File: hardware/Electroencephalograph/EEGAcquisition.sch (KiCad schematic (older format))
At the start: 52 parts, among them U1 ADS1298IPAG, U2 OPA330xxD, U4 REF5025, U5 OPA350, X1 2M048

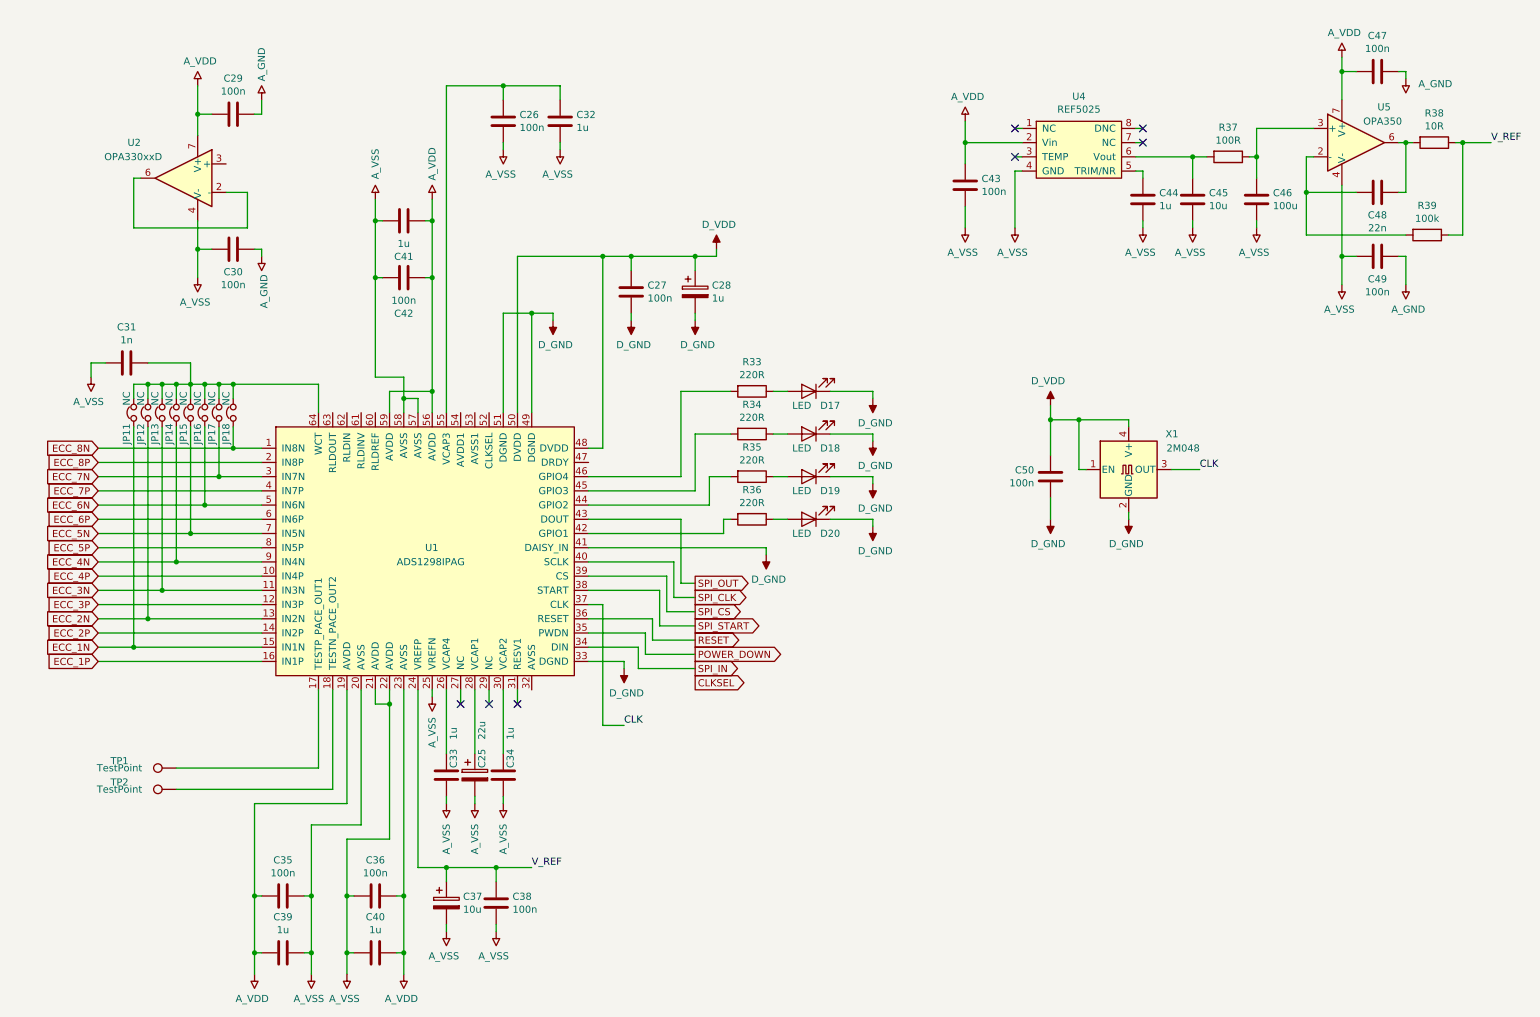
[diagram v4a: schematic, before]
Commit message: removed external clk and vref
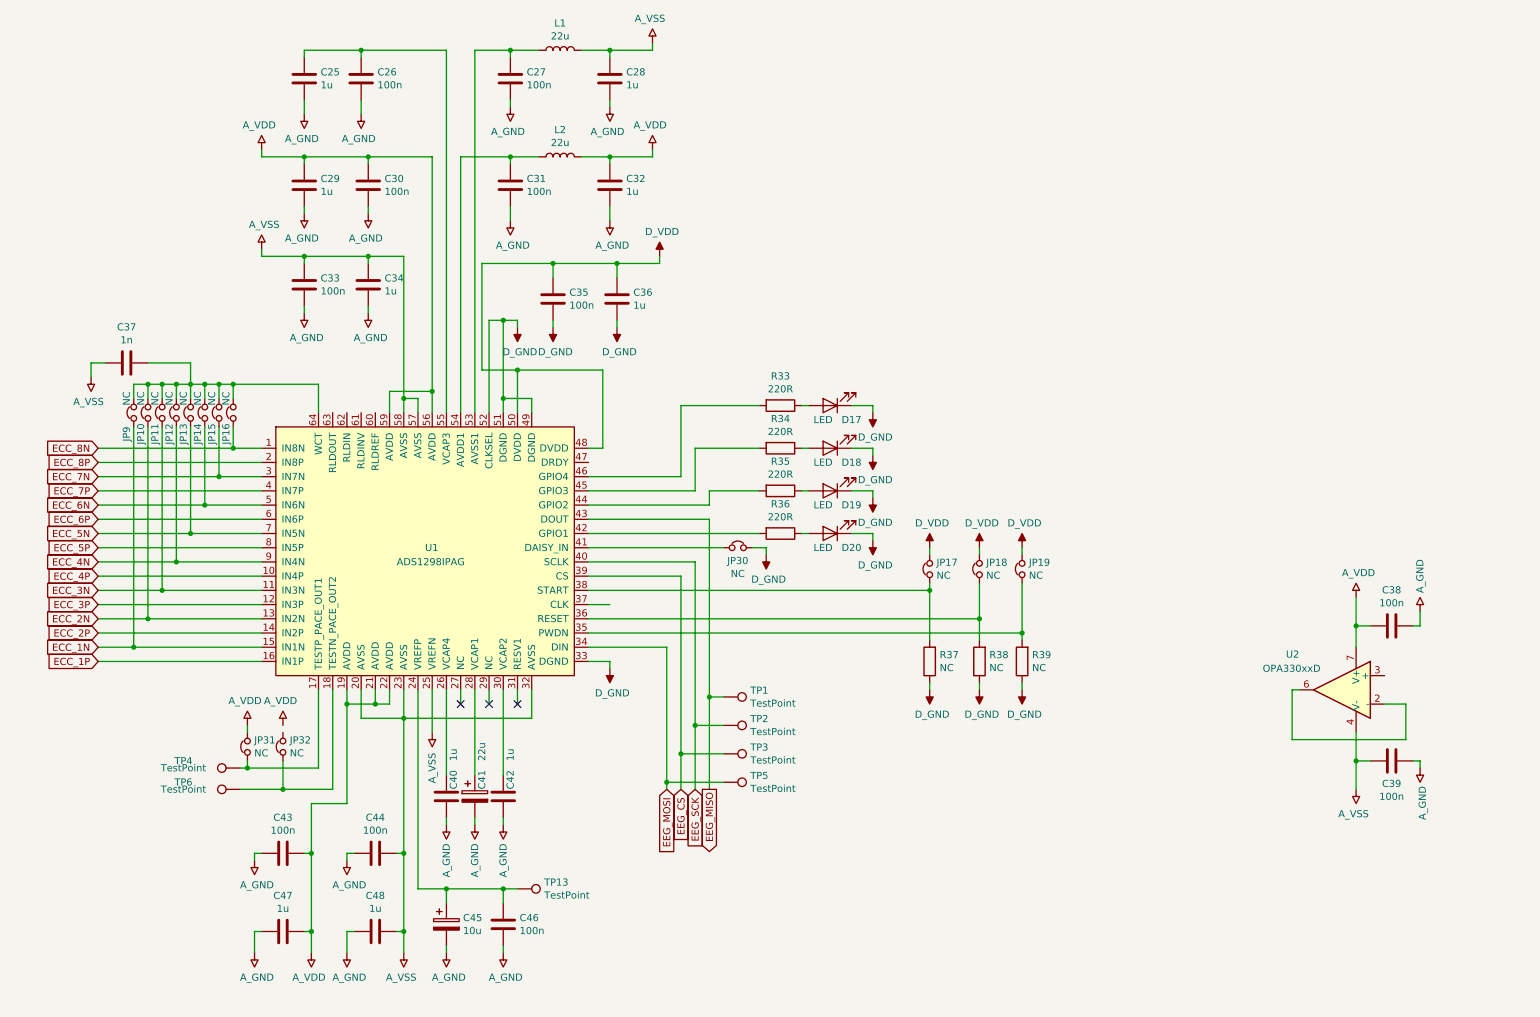
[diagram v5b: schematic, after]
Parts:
- removed C28: 1u, Capacitor_Tantalum_SMD:CP_EIA-3528-21_Kemet-B, symbol Device:CP
- removed C41, C44: 1u, Capacitor_SMD:C_0402_1005Metric, symbol Device:C
- removed C42, C43, C47, C49, C50: 100n, Capacitor_SMD:C_0402_1005Metric, symbol Device:C
- removed C45: 10u, Capacitor_SMD:C_0402_1005Metric, symbol Device:C
- removed C46: 100u, Capacitor_SMD:C_0402_1005Metric, symbol Device:C
- removed C48: 22n, Capacitor_SMD:C_0402_1005Metric, symbol Device:C
- removed U4: REF5025, Package_SO:VSSOP-8_2.3x2mm_P0.5mm, symbol Electroencephalograph:REF5025
- removed U5: OPA350, Package_SO:SOIC-8_3.9x4.9mm_P1.27mm, symbol Electroencephalograph:OPA350
- removed X1: 2M048, Oscillator:Oscillator_SMD_EuroQuartz_XO53-4Pin_5.0x3.2mm, symbol Oscillator:XO91
- added C27, C30, C31, C33: 100n, Capacitor_SMD:C_0402_1005Metric, symbol Device:C
- added C28, C29, C32, C34, C36: 1u, Capacitor_SMD:C_0402_1005Metric, symbol Device:C
- added JP17, JP18, JP19, JP30, JP31, JP32: NC, Jumper:SolderJumper-2_P1.3mm_Bridged_Pad1.0x1.5mm, symbol Device:Jumper_NC_Small
- added L1: 22u, Inductor_SMD:L_7.3x7.3_H3.5, symbol Device:L
- added L2: 22u, Inductor_SMD:L_1206_3216Metric, symbol Device:L
- added TP1, TP13, TP2, TP3, TP5: TestPoint, TestPoint:TestPoint_Pad_1.5x1.5mm, symbol Connector:TestPoint
- R37: value 100R -> NC
- R38: value 10R -> NC
- R39: value 100k -> NC
- U1: Vendor (none) -> xxx
- renumbered C32 to C25, C27 to C35, C31 to C37, C29 to C38, C30 to C39, C33 to C40, C25 to C41, C34 to C42, C35 to C43, C36 to C44, C37 to C45, C38 to C46, C39 to C47, C40 to C48, JP12 to JP10, JP13 to JP11, JP14 to JP12, JP15 to JP13, JP16 to JP14, JP17 to JP15, JP18 to JP16, JP11 to JP9, TP1 to TP4, TP2 to TP6
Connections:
- net POWER_DOWN is gone; now on an unnamed net: U1.35 (PWDN)
- net RESET is gone; now on an unnamed net: U1.36 (RESET)
- net SPI_START is gone; now on an unnamed net: U1.38 (START)
- net GNDA: now also C25.2, C26.2, C40.2, C41.2, C42.2, C43.2, C44.2, C45.2, C46.2, C47.2, C48.2, R37.1, R38.1, R39.1, U1.52 (CLKSEL), C27.1, C28.1, C29.1, C30.1, C31.2, C32.2, C33.1, C34.1, C36.2, JP30.1; no longer U1.41 (DAISY_IN)
- net VDDA: now also U1.32 (AVSS), C28.2, C29.2, C30.2, C32.1, C33.2, C34.2, C36.1, JP17.1, JP18.1, JP19.1, JP31.1, L1.2, L2.2; no longer C25.2, C26.2, C40.2, C41.2, C42.2, C43.2, C44.2, C45.2, C46.2, C47.2, C48.2
- net at TP4.1, U1.17 (TESTP_PACE_OUT1): now also JP31.2
- net at TP6.1, U1.18 (TESTN_PACE_OUT2): now also JP32.2
- net at U1.53 (AVSS1): now also C27.2, L1.1
- net at U1.54 (AVDD1): now also C31.1, L2.1
- net at R37.2: now also JP17.2
- net at R39.2: now also JP19.2
- net at R38.2: now also JP18.2
- net CLK: no longer names the net of U1.37 (CLK)
- net SPI_CLK renamed EEG_SCK
- net EEG_SCK: now also TP2.1
- net SPI_CS renamed EEG_CS
- net EEG_CS: now also TP3.1
- net SPI_IN renamed EEG_MOSI
- net EEG_MOSI: now also TP5.1
- net SPI_OUT renamed EEG_MISO
- net EEG_MISO: now also TP1.1
- net V_REF: no longer names the net of C45.1, C46.1, U1.24 (VREFP)
- net V_REF: now also TP13.1; no longer R38.1, R39.1
- new net: JP30.2, U1.41 (DAISY_IN)
- no-connect marks 7 -> 3
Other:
- moved on the sheet: C25, C26, C35, C38, C39, C40, C41, C42, C43, C44, C45, C46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

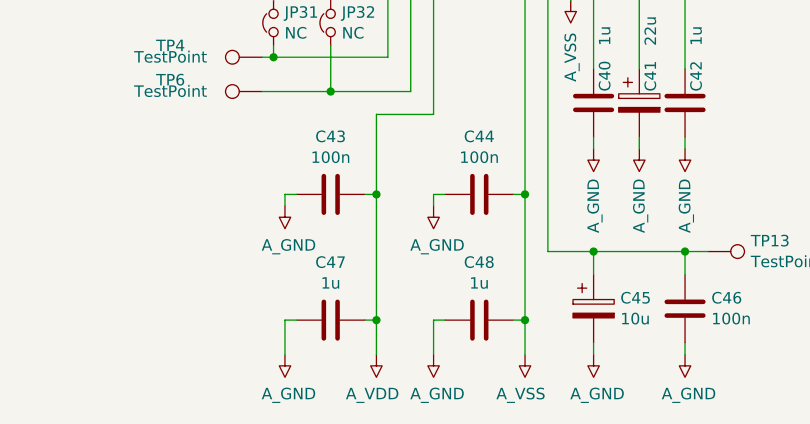
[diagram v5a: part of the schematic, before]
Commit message: bom simplification
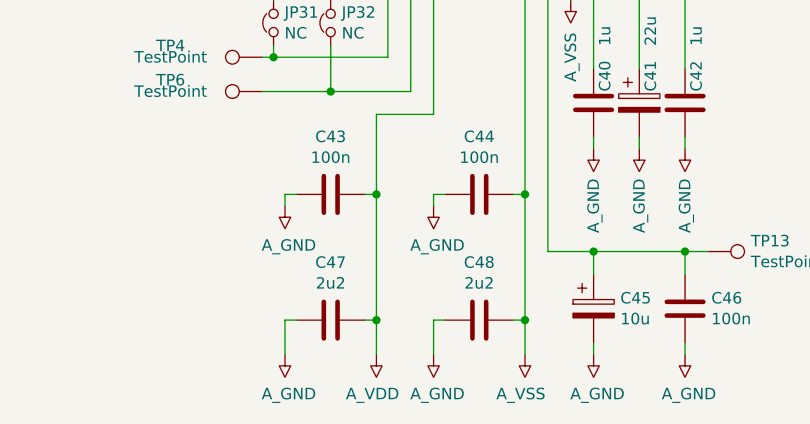
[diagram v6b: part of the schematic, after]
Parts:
- C47, C48: value 1u -> 2u2
- L2: footprint Inductor_SMD:L_1206_3216Metric -> Inductor_SMD:L_7.3x7.3_H3.5
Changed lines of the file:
@@
 AR Path="/5DF61103/5E1F8BAE" Ref="C48"  Part="1"
 F 0 "C48" V 2748 7000 50  0000 C CNN
-F 1 "1u" V 2839 7000 50  0000 C CNN
+F 1 "2u2" V 2839 7000 50  0000 C CNN
 F 2 "Capacitor_SMD:C_0402_1005Metric" H 3038 6850 50  0001 C CNN
 F 3 "~" H 3000 7000 50  0001 C CNN
@@
 AR Path="/5DF61103/5E267921" Ref="C47"  Part="1"
 F 0 "C47" V 2098 7000 50  0000 C CNN
-F 1 "1u" V 2189 7000 50  0000 C CNN
+F 1 "2u2" V 2189 7000 50  0000 C CNN
 F 2 "Capacitor_SMD:C_0402_1005Metric" H 2388 6850 50  0001 C CNN
 F 3 "~" H 2350 7000 50  0001 C CNN
@@
 F 0 "L2" V 4490 1550 50  0000 C CNN
 F 1 "22u" V 4399 1550 50  0000 C CNN
-F 2 "Inductor_SMD:L_1206_3216Metric" H 4300 1550 50  0001 C CNN
+F 2 "Inductor_SMD:L_7.3x7.3_H3.5" H 4300 1550 50  0001 C CNN
 F 3 "~" H 4300 1550 50  0001 C CNN
 	1    4300 1550

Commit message: draft of PCB routing
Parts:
- renumbered C37 to C25, C43 to C26, C47 to C27, C25 to C28, C33 to C30, C26 to C31, C30 to C32, C34 to C33, C44 to C34, C48 to C35, C40 to C36, C45 to C37, C41 to C38, C42 to C39, C46 to C40, C27 to C41, C31 to C42, C35 to C43, C28 to C44, C32 to C45, C36 to C46, C38 to C47, C39 to C48, JP31 to JP17, JP32 to JP18, JP30 to JP19, JP17 to JP20, JP18 to JP21, JP19 to JP22, TP4 to TP1, TP6 to TP2, TP13 to TP3, TP1 to TP4, TP2 to TP5, TP3 to TP6, TP5 to TP7
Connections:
- net OPAMP_MAYBE: now reaches U1.61 (RLDINV)
- net OPAMP_MAYBE: now also U2.2 (-), U2.6

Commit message: added inductor 3d model
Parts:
- L1, L2: footprint Inductor_SMD:L_7.3x7.3_H3.5 -> Electroencephalograph:L_7.3x7.3_H3.5
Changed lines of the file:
@@
 F 0 "L1" V 4490 800 50  0000 C CNN
 F 1 "22u" V 4399 800 50  0000 C CNN
-F 2 "Inductor_SMD:L_7.3x7.3_H3.5" H 4300 800 50  0001 C CNN
+F 2 "Electroencephalograph:L_7.3x7.3_H3.5" H 4300 800 50  0001 C CNN
 F 3 "~" H 4300 800 50  0001 C CNN
 	1    4300 800
@@
 F 0 "L2" V 4490 1550 50  0000 C CNN
 F 1 "22u" V 4399 1550 50  0000 C CNN
-F 2 "Inductor_SMD:L_7.3x7.3_H3.5" H 4300 1550 50  0001 C CNN
+F 2 "Electroencephalograph:L_7.3x7.3_H3.5" H 4300 1550 50  0001 C CNN
 F 3 "~" H 4300 1550 50  0001 C CNN
 	1    4300 1550
